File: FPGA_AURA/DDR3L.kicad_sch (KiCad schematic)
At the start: 42 parts, among them U500 MT41K128M16JT-125_IT_K

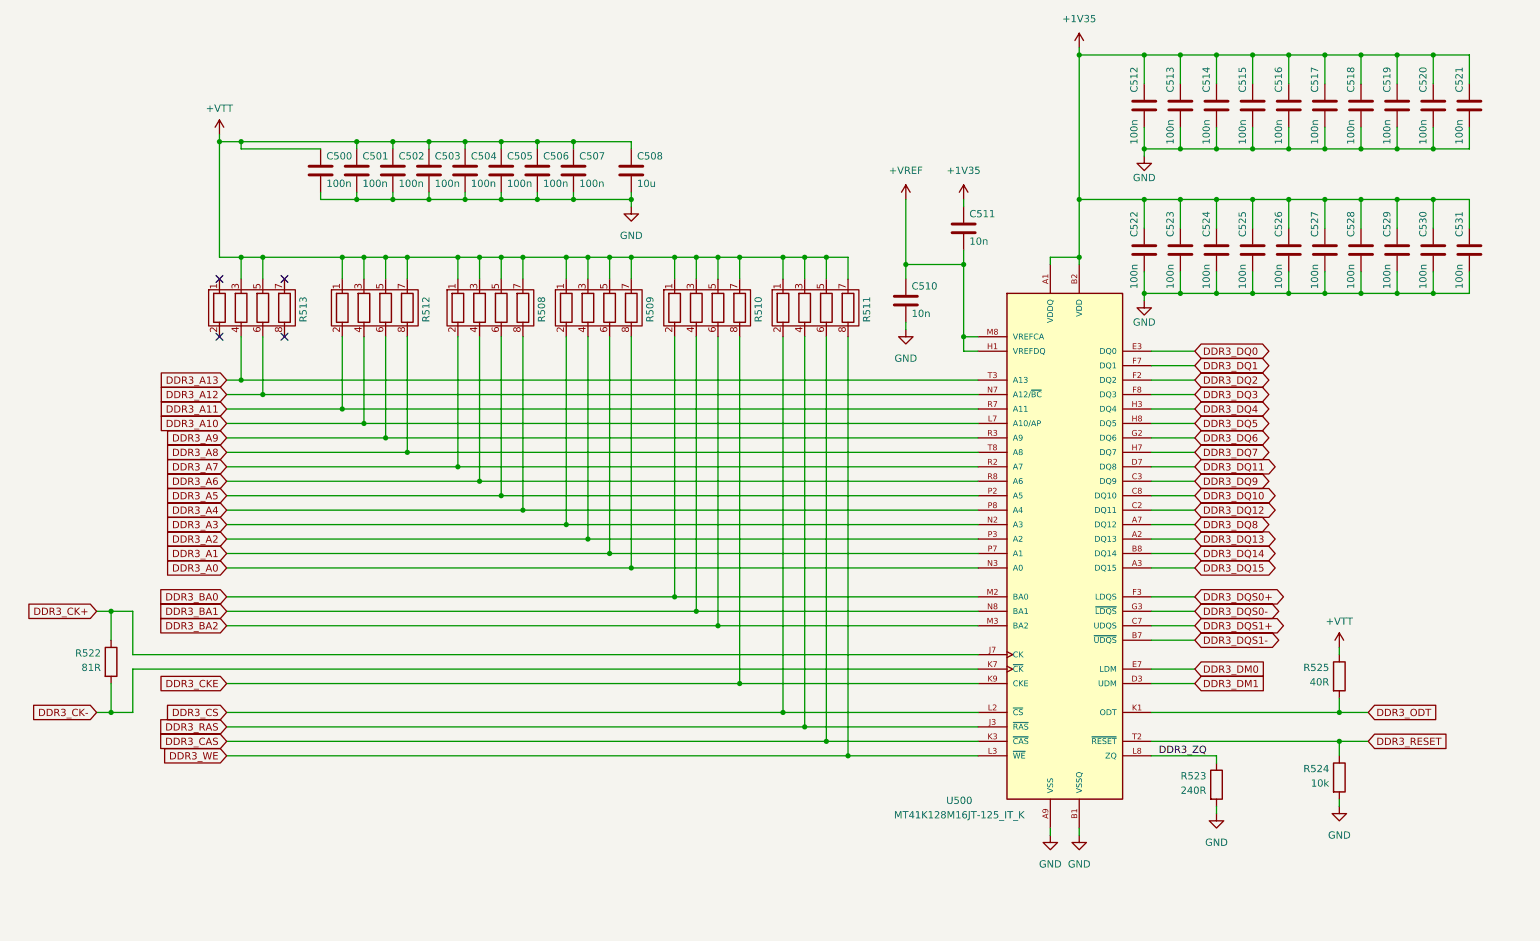
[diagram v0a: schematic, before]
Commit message: Finished schematic to start routing again, and started MII fanout from connector.
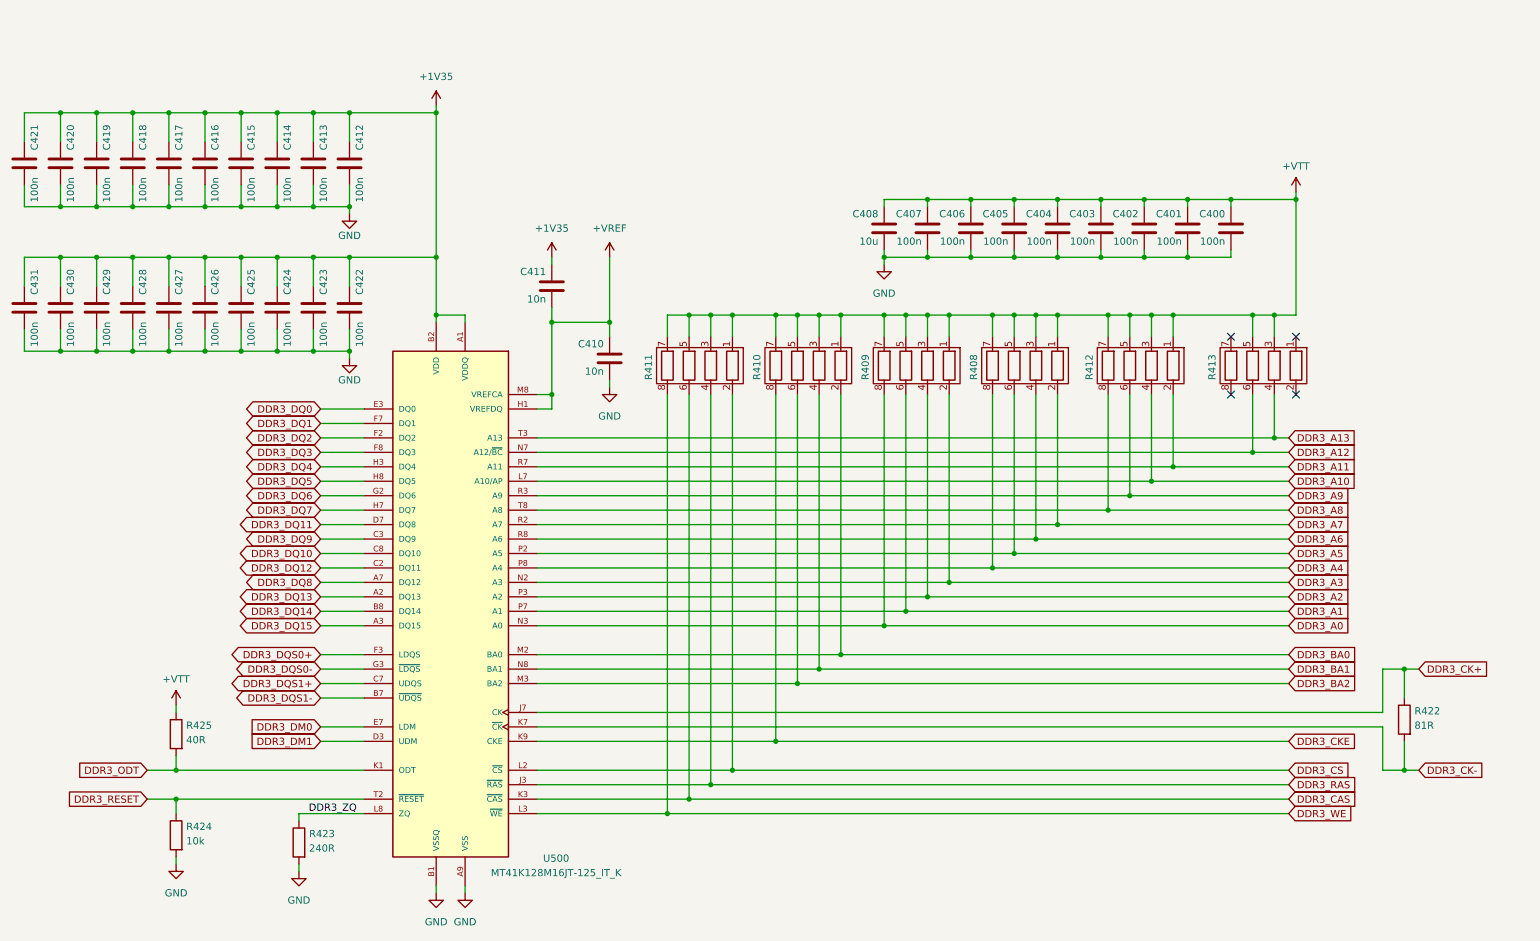
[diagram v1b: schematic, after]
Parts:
- renumbered C500 to C400, C501 to C401, C502 to C402, C503 to C403, C504 to C404, C505 to C405, C506 to C406, C507 to C407, C508 to C408, C510 to C410, C511 to C411, C512 to C412, C513 to C413, C514 to C414, C515 to C415, C516 to C416, C517 to C417, C518 to C418, C519 to C419, C520 to C420, C521 to C421, C522 to C422, C523 to C423, C524 to C424, C525 to C425, C526 to C426, C527 to C427, C528 to C428, C529 to C429, C530 to C430, C531 to C431, R508 to R408, R509 to R409, R510 to R410, R511 to R411, R512 to R412, R513 to R413, R522 to R422, R523 to R423, R524 to R424, R525 to R425
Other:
- company: (none) -> Alexander Armitage
- title: (none) -> DDR3L
- moved on the sheet: C400, C401, C402, C403, C404, C405, C406, C407, C408, C410, C411, C412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

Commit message: All components placed, routing left to do followed by final checks.
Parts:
- C414, C416, C419, C423, C425, C426, C427, C428, C430: footprint Capacitor_SMD:C_0402_1005Metric -> Capacitor_SMD:C_0201_0603Metric
- R422: value 81R -> 91R; footprint Resistor_SMD:R_0402_1005Metric -> Resistor_SMD:R_0201_0603Metric
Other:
- moved on the sheet: C414, C415, C416, C417, C418, C419, C420, C421, C423, C424, C425, C426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

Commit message: Finishing off routing, fanning out fly by termination, and added ground pours
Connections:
- net +VREF renamed +VREF_DDR
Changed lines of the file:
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@@
 			)
 		)
-		(property "Value" "+VREF"
-			(at 123.19 52.07 0)
+		(property "Value" "+VREF_DDR"
+			(at 125.73 55.8799 0)
 			(show_name no)
 			(do_not_autoplace no)
@@
 					(size 1.27 1.27)
 				)
+				(justify right)
 			)
 		)

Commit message: Schematic initial draft complete.
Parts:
- C400, C401, C402, C403, C404, C405, C406, C407: value 100n -> 1u
- R408, R409, R410, R411, R412, R413: value (none) -> 40R2
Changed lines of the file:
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@@
 			)
 		)
-		(property "Value" "100n"
+		(property "Value" "1u"
 			(at 208.534 54.356 0)
 			(show_name no)
@@
 			)
 		)
-		(property "Value" "100n"
+		(property "Value" "1u"
 			(at 223.774 54.356 0)
 			(show_name no)
@@
 			)
 		)
-		(property "Value" ""
+		(property "Value" "40R2"
 			(at 229.87 77.47 0)
+			(hide yes)
 			(show_name no)
 			(do_not_autoplace no)
@@
 			)
 		)
-		(property "Value" "100n"
+		(property "Value" "1u"
 			(at 185.674 54.356 0)
 			(show_name no)
@@
 			)
 		)
-		(property "Value" "100n"
+		(property "Value" "1u"
 			(at 231.394 54.356 0)
 			(show_name no)
@@
 			)
 		)
-		(property "Value" ""
+		(property "Value" "40R2"
 			(at 130.81 77.47 0)
+			(hide yes)
 			(show_name no)
 			(do_not_autoplace no)
@@
 			)
 		)
-		(property "Value" ""
+		(property "Value" "40R2"
 			(at 208.28 77.47 0)
+			(hide yes)
 			(show_name no)
 			(do_not_autoplace no)
@@
 			)
 		)
-		(property "Value" "100n"
+		(property "Value" "1u"
 			(at 200.914 54.356 0)
 			(show_name no)
@@
 			)
 		)
-		(property "Value" "100n"
+		(property "Value" "1u"
 			(at 193.294 54.356 0)
 			(show_name no)
@@
 			)
 		)
-		(property "Value" "100n"
+		(property "Value" "1u"
 			(at 178.054 54.356 0)
 			(show_name no)
@@
 			)
 		)
-		(property "Value" ""
+		(property "Value" "40R2"
 			(at 187.96 77.47 0)
+			(hide yes)
 			(show_name no)
 			(do_not_autoplace no)
@@
 			)
 		)
-		(property "Value" ""
+		(property "Value" "40R2"
 			(at 149.86 77.47 0)
+			(hide yes)
 			(show_name no)
 			(do_not_autoplace no)
@@
 			)
 		)
-		(property "Value" "100n"
+		(property "Value" "1u"
 			(at 216.154 54.356 0)
 			(show_name no)
@@
 			)
 		)
-		(property "Value" ""
+		(property "Value" "40R2"
 			(at 168.91 77.47 0)
+			(hide yes)
 			(show_name no)
 			(do_not_autoplace no)

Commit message: Connected all DDR3 bar the reset pin and routed all decoupling caps.
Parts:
- added R426: 40R, Resistor_SMD:R_0201_0603Metric, symbol Device:R
- C415, C418, C420, C424, C429: footprint Capacitor_SMD:C_0402_1005Metric -> Capacitor_SMD:C_0201_0603Metric
- R425: footprint Resistor_SMD:R_0402_1005Metric -> Resistor_SMD:R_0201_0603Metric
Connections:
- net +VTT: now also R413.1, R413.7, R426.1
- net DDR3_A0: now also R413.6; no longer R409.8
- net DDR3_A1: now also R408.2; no longer R409.6
- net DDR3_A10: now also R410.6; no longer R412.4
- net DDR3_A11: now also R408.4; no longer R412.2
- net DDR3_A12: now also R408.6; no longer R413.6
- net DDR3_A13: now also R411.8; no longer R413.4
- net DDR3_A2: now also R411.4; no longer R409.4
- net DDR3_A3: now also R413.4; no longer R409.2
- net DDR3_A4: now also R412.6; no longer R408.8
- net DDR3_A5: now also R413.8; no longer R408.6
- net DDR3_A6: now also R412.4; no longer R408.4
- net DDR3_A7: now also R411.2; no longer R408.2
- net DDR3_A8: now also R408.8; no longer R412.8
- net DDR3_A9: now also R411.6; no longer R412.6
- net DDR3_BA0: now also R409.8; no longer R410.2
- net DDR3_BA2: now also R413.2; no longer R410.6
- net DDR3_CAS: now also R409.2; no longer R411.6
- net DDR3_CS: now also R409.6; no longer R411.2
- net DDR3_RAS: now also R426.2; no longer R411.4
- net DDR3_WE: now also R409.4; no longer R411.8
- no-connect marks 4 -> 3
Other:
- moved on the sheet: R422
